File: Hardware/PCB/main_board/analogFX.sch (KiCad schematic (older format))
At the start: 16 parts, among them Q1 BC547, U1 MCP6002-xSN

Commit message: Place HMI
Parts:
- added BAR1: HDSP-4840_2, Display:HDSP-4840, symbol LED:HDSP-4840_2
- added RV_DIST_DRIVE1, RV_DIST_MIX1, RV_DIST_TONE1: 10k, Potentiometer_THT:Potentiometer_Alps_RK09K_Single_Vertical, symbol Device:R_POT
- added RV_VOL1: R_POT_Dual, Potentiometer_THT:Potentiometer_Alps_RK09L_Double_Vertical, symbol Device:R_POT_Dual
- renumbered RV1 to RV_HPF_CUT1, RV2 to RV_HPF_RES1
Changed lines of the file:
@@
 $Descr A4 11693 8268
 encoding utf-8
-Sheet 3 7
+Sheet 6 7
 Title ""
 Date ""
@@
 P 1550 1450
 AR Path="/5E64D300" Ref="RV?"  Part="1"
-AR Path="/5E632F77/5E64D300" Ref="RV1"  Part="1"
-F 0 "RV1" H 1480 1496 50  0000 R CNN
+AR Path="/5E632F77/5E64D300" Ref="RV_HPF_CUT1"  Part="1"
+F 0 "RV_HPF_CUT1" H 1480 1496 50  0000 R CNN
 F 1 "10k" H 1480 1405 50  0000 R CNN
 F 2 "Potentiometer_THT:Potentiometer_Alps_RK09K_Single_Vertical" H 1550 1450 50  0001 C CNN
@@
 P 4300 1250
 AR Path="/5E64D312" Ref="RV?"  Part="1"
-AR Path="/5E632F77/5E64D312" Ref="RV2"  Part="1"
-F 0 "RV2" V 4185 1250 50  0000 C CNN
+AR Path="/5E632F77/5E64D312" Ref="RV_HPF_RES1"  Part="1"
+F 0 "RV_HPF_RES1" V 4185 1250 50  0000 C CNN
 F 1 "10k" V 4094 1250 50  0000 C CNN
 F 2 "Potentiometer_THT:Potentiometer_Alps_RK09K_Single_Vertical" H 4300 1250 50  0001 C CNN
@@
 Wire Wire Line
 	2800 4400 3100 4400
+$Comp
+L Device:R_POT RV?
+U 1 1 5E58F714
+P 7850 1950
+AR Path="/5E58F714" Ref="RV?"  Part="1"
+AR Path="/5E632F77/5E58F714" Ref="RV_DIST_DRIVE1"  Part="1"
+F 0 "RV_DIST_DRIVE1" V 7735 1950 50  0000 C CNN
+F 1 "10k" V 7644 1950 50  0000 C CNN
+F 2 "Potentiometer_THT:Potentiometer_Alps_RK09K_Single_Vertical" H 7850 1950 50  0001 C CNN
+F 3 "~" H 7850 1950 50  0001 C CNN
+	1    7850 1950
+	0    -1   -1   0
+$EndComp
+$Comp
+L Device:R_POT RV?
+U 1 1 5E590192
+P 8450 1950
+AR Path="/5E590192" Ref="RV?"  Part="1"
+AR Path="/5E632F77/5E590192" Ref="RV_DIST_TONE1"  Part="1"
+F 0 "RV_DIST_TONE1" V 8335 1950 50  0000 C CNN
+F 1 "10k" V 8244 1950 50  0000 C CNN
+F 2 "Potentiometer_THT:Potentiometer_Alps_RK09K_Single_Vertical" H 8450 1950 50  0001 C CNN
+F 3 "~" H 8450 1950 50  0001 C CNN
+	1    8450 1950
+	0    -1   -1   0
+$EndComp
+$Comp
+L Device:R_POT RV?
+U 1 1 5E59052A
+P 9000 1950
+AR Path="/5E59052A" Ref="RV?"  Part="1"
+AR Path="/5E632F77/5E59052A" Ref="RV_DIST_MIX1"  Part="1"
+F 0 "RV_DIST_MIX1" V 8885 1950 50  0000 C CNN
+F 1 "10k" V 8794 1950 50  0000 C CNN
+F 2 "Potentiometer_THT:Potentiometer_Alps_RK09K_Single_Vertical" H 9000 1950 50  0001 C CNN
+F 3 "~" H 9000 1950 50  0001 C CNN
+	1    9000 1950
+	0    -1   -1   0
+$EndComp
+$Comp
+L Device:R_POT_Dual RV_VOL1
+U 1 1 5E599706
+P 8400 2650
+F 0 "RV_VOL1" H 8400 2417 50  0000 C CNN
+F 1 "R_POT_Dual" H 8400 2326 50  0000 C CNN
+F 2 "Potentiometer_THT:Potentiometer_Alps_RK09L_Double_Vertical" H 8650 2575 50  0001 C CNN
+F 3 "~" H 8650 2575 50  0001 C CNN
+	1    8400 2650
+	1    0    0    -1
+$EndComp
+$Comp
+L LED:HDSP-4840_2 BAR1
+U 1 1 5E5A0C61
+P 8350 4250
+F 0 "BAR1" H 8350 4917 50  0000 C CNN
+F 1 "HDSP-4840_2" H 8350 4826 50  0000 C CNN
+F 2 "Display:HDSP-4840" H 8350 3450 50  0001 C CNN
+F 3 "https://docs.broadcom.com/docs/AV02-1798EN" H 6350 4450 50  0001 C CNN
+	1    8350 4250
+	1    0    0    -1
+$EndComp
 $EndSCHEMATC

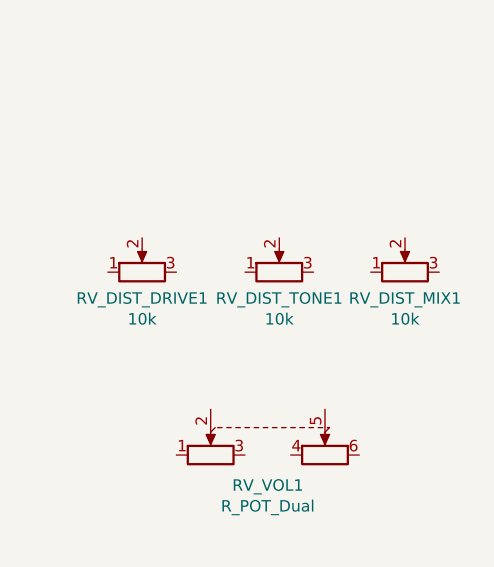
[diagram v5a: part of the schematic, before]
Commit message: Place connectors
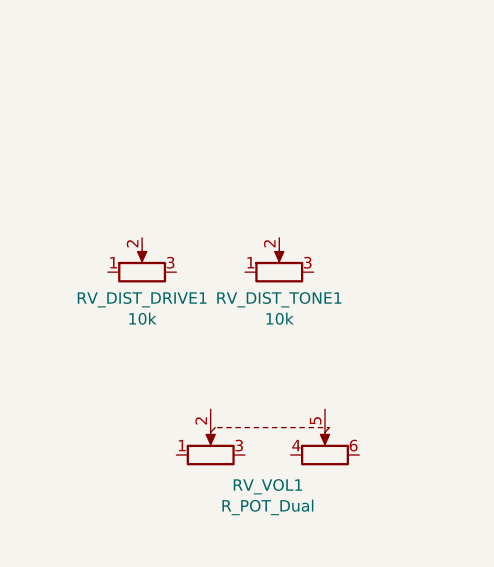
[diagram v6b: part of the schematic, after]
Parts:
- removed RV_DIST_MIX1: 10k, Potentiometer_THT:Potentiometer_Alps_RK09K_Single_Vertical, symbol Device:R_POT
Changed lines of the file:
@@
-$EndComp
-$Comp
-L Device:R_POT RV?
-U 1 1 5E59052A
-P 9000 1950
-AR Path="/5E59052A" Ref="RV?"  Part="1"
-AR Path="/5E632F77/5E59052A" Ref="RV_DIST_MIX1"  Part="1"
-F 0 "RV_DIST_MIX1" V 8885 1950 50  0000 C CNN
-F 1 "10k" V 8794 1950 50  0000 C CNN
-F 2 "Potentiometer_THT:Potentiometer_Alps_RK09K_Single_Vertical" H 9000 1950 50  0001 C CNN
-F 3 "~" H 9000 1950 50  0001 C CNN
-	1    9000 1950
-	0    -1   -1   0
 $EndComp
 $Comp

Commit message: Route PWR
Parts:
- added C15: 47p, Capacitor_SMD:C_0805_2012Metric, symbol Device:C
- added C16, C21: 1u, Capacitor_SMD:C_0805_2012Metric, symbol Device:C
- added C17: 51p, Capacitor_SMD:C_0805_2012Metric, symbol Device:C
- added C18, C19: 220n, Capacitor_SMD:C_0805_2012Metric, symbol Device:C
- added C20: 100n, Capacitor_SMD:C_0805_2012Metric, symbol Device:C
- added D2, D3: 1N4148W, Diode_SMD:D_SOD-123, symbol Diode:1N4148W
- added R10: 4.7k, Resistor_SMD:R_0805_2012Metric, symbol Device:R
- added R11, R12, R13, R17: 10k, Resistor_SMD:R_0805_2012Metric, symbol Device:R
- added R14: 500, Resistor_SMD:R_0805_2012Metric, symbol Device:R
- added R15, R18, R19: 1k, Resistor_SMD:R_0805_2012Metric, symbol Device:R
- added R16: 220, Resistor_SMD:R_0805_2012Metric, symbol Device:R
- added U4: RC4558, Package_SO:SOIC-8_3.9x4.9mm_P1.27mm, symbol Amplifier_Operational:RC4558
- C5: value 4.7u -> 100n
- RV_DIST_DRIVE1: value 10k -> 500k log
- RV_DIST_TONE1: value 10k -> 22k
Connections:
- net +5VA: now also C20.2, R11.1, U4.8 (V+)
- net AUDIO_OUT: now also R19.2; no longer C4.1
- net GND: now also C18.2, C20.1, R10.2, R13.1, R16.2, U4.4 (V-)
- net at RV_DIST_DRIVE1.1: now also R14.1
- net at RV_DIST_DRIVE1.2: now also RV_DIST_DRIVE1.3, C17.1, D2.2 (A), D3.1 (K), R15.1, U4.1
- net at RV_DIST_TONE1.1: now also C18.1, R15.2, R17.1, U4.5 (+)
- net at RV_DIST_TONE1.2: now also C19.1
- net at RV_DIST_TONE1.3: now also R18.1, U4.6 (-)
- new net: C15.1, C17.2, D2.1 (K), D3.2 (A), R14.2, U4.2 (-)
- new net: C16.1, R12.2, U4.3 (+)
- new net: C21.2, R18.2, U4.7
- new net: C15.2, R10.1
- new net: R11.2, R12.1, R13.2, R17.2
- new net: C19.2, R16.1
- new net: C21.1, R19.1
- new net OUT_VCF__IN_DIST: C16.2, C4.1
- no-connect marks 0 -> 26
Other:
- note added: "Distortion"
- moved on the sheet: BAR1, RV_DIST_DRIVE1, RV_DIST_TONE1, RV_VOL1, U1B
